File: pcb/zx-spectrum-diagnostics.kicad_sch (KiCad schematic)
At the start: 18 parts, among them J101 Conn_01x04, J102 Conn_01x03_Male, J103 Conn_01x03_Male, Q101 PMBT2222A, SW101 SW_SPST, U101 Pico, U102 Pico

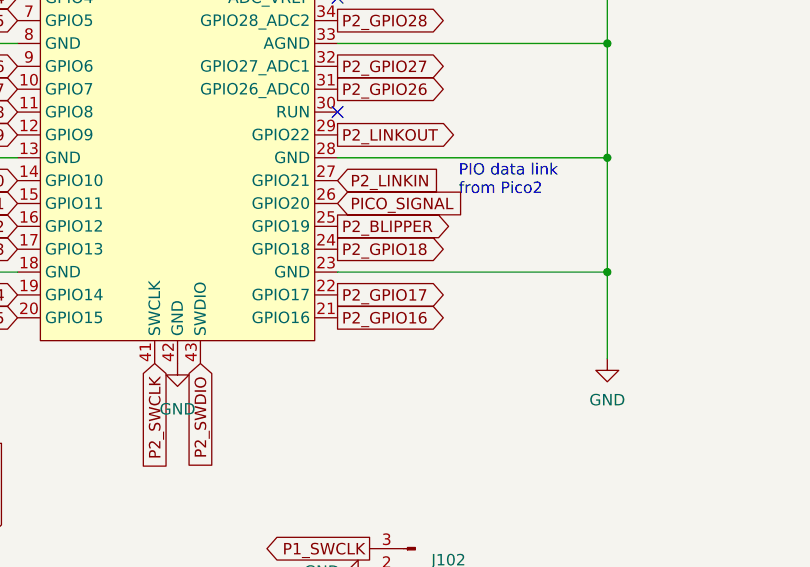
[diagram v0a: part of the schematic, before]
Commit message: basic comms between the picos established
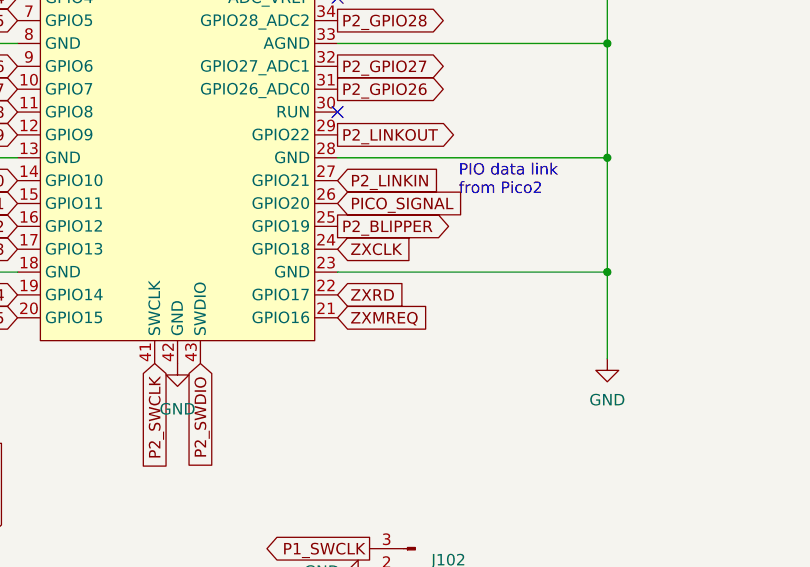
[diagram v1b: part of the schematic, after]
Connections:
- net P2_GPIO16 is gone; now on net ZXMREQ: U102.21 (GPIO16)
- net P2_GPIO17 is gone; now on net ZXRD: U102.22 (GPIO17)
- net P2_GPIO18 is gone; now on net ZXCLK: U102.24 (GPIO18)
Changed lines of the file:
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@@
     )
   )
-  (global_label "P2_GPIO17" (shape output) (at 148.336 148.59 0) (fields_autoplaced)
-    (effects (font (size 1.27 1.27)) (justify left))
-    (property "Intersheet References" "${INTERSHEET_REFS}" (id 0) (at 161.0905 148.5106 0)
+  (global_label "ZXRD" (shape input) (at 148.336 148.59 0) (fields_autoplaced)
+    (effects (font (size 1.27 1.27)) (justify left))
+    (property "Intersheet References" "${INTERSHEET_REFS}" (id 0) (at 155.7081 148.5106 0)
       (effects (font (size 1.27 1.27)) (justify left) hide)
     )
@@
     )
   )
-  (global_label "P2_GPIO18" (shape output) (at 148.336 143.51 0) (fields_autoplaced)
-    (effects (font (size 1.27 1.27)) (justify left))
-    (property "Intersheet References" "${INTERSHEET_REFS}" (id 0) (at 161.0905 143.4306 0)
+  (global_label "ZXCLK" (shape input) (at 148.336 143.51 0) (fields_autoplaced)
+    (effects (font (size 1.27 1.27)) (justify left))
+    (property "Intersheet References" "${INTERSHEET_REFS}" (id 0) (at 156.7362 143.4306 0)
       (effects (font (size 1.27 1.27)) (justify left) hide)
     )
@@
     )
   )
-  (global_label "P2_GPIO16" (shape output) (at 148.336 151.13 0) (fields_autoplaced)
-    (effects (font (size 1.27 1.27)) (justify left))
-    (property "Intersheet References" "${INTERSHEET_REFS}" (id 0) (at 161.0905 151.0506 0)
-      (effects (font (size 1.27 1.27)) (justify left) hide)
-    )
+  (global_label "ZXMREQ" (shape input) (at 148.336 151.13 0) (fields_autoplaced)
+    (effects (font (size 1.27 1.27)) (justify left))
+    (property "Intersheet References" "${INTERSHEET_REFS}" (id 0) (at 158.3691 151.0506 0)
+      (effects (font (size 1.27 1.27)) (justify left) hide)
+    )
